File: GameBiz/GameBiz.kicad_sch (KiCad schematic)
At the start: 33 parts

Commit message: initial schematic is finished
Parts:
- removed C? (x2): 10uF, symbol Device:C
- removed L?: 2.2 uH, symbol Device:L
- removed R?: 162K, symbol Device:R
- removed R?: 100K, symbol Device:R
- removed R?: 5.1K, symbol Device:R
- removed S?: RUN, symbol Eclectronics:SW
- removed U?: ADP1607ACPZN001-R7, CP_6_3_ADI, symbol ADP1607ACPZN001:ADP1607ACPZN001-R7
- removed U?: RP2040, Package_DFN_QFN:QFN-56-1EP_7x7mm_P0.4mm_EP3.2x3.2mm, symbol MCU_RaspberryPi:RP2040
- added AE1: Antenna_Loop, Footprints:2_4GHZANTENNA, symbol Device:Antenna_Loop
- added C1, C10, C11, C2, C3, C4, C5, C6, C7, C8, C9: 0.1uF, Capacitor_SMD:C_0603_1608Metric, symbol Device:C
- added C14: 4.7uF, Capacitor_SMD:C_0603_1608Metric, symbol Device:C
- added C16, C18, C20: 100pF, Capacitor_SMD:C_0603_1608Metric, symbol Device:C
- added C17, C19: 2.2uF, Capacitor_SMD:C_0603_1608Metric, symbol Device:C
- added C21: 33nF, Capacitor_SMD:C_0603_1608Metric, symbol Device:C
- added C22: 22uF, Capacitor_SMD:C_0603_1608Metric, symbol Device:C
- added C23: 10nF, Capacitor_SMD:C_0603_1608Metric, symbol Device:C
- added C24: 1nF, Capacitor_SMD:C_0603_1608Metric, symbol Device:C
- added C25, C26: 1uF, Capacitor_SMD:C_0603_1608Metric, symbol Device:C
- added C27: 2.2nF, Capacitor_SMD:C_0603_1608Metric, symbol Device:C
- added C29: 4.7pF, Capacitor_SMD:C_0603_1608Metric, symbol Device:C
- added C30: 1.5pF, Capacitor_SMD:C_0603_1608Metric, symbol Device:C
- added C31: 1pF, Capacitor_SMD:C_0603_1608Metric, symbol Device:C
- added C32: 10uF, Capacitor_SMD:C_0603_1608Metric, symbol Device:C
- added C33, C34: 22pF, Capacitor_SMD:C_0603_1608Metric, symbol Device:C
- added L1: 2.7nH, Inductor_SMD:L_0603_1608Metric, symbol Device:L
- added L2: 3.9nH, Inductor_SMD:L_0603_1608Metric, symbol Device:L
- added L3: 8.2nH, Inductor_SMD:L_0603_1608Metric, symbol Device:L
- added L4: 3.3uH, Inductor_SMD:L_0603_1608Metric, symbol Device:L
- added Q1: PMCXB900UEZ, Footprints:PMCXB900UEZ, symbol PMCXB900UEZ:PMCXB900UEZ
- added R12, R13, R14, R15, R16, R17, R18, R19: 470, Resistor_SMD:R_0603_1608Metric, symbol Device:R
- added R2, R3: 5.1K, Resistor_SMD:R_0603_1608Metric, symbol Device:R
- added R20: 1M, Resistor_SMD:R_0603_1608Metric, symbol Device:R
- added R8: 22K, Resistor_SMD:R_0603_1608Metric, symbol Device:R
- added S1: RST, Footprints:KXT321LHS, symbol Eclectronics:SW
- added S10, S3, S4, S5, S6, S7, S8, S9: SW, Footprints:capacitivetouch, symbol Eclectronics:SW
- added S2: BOOT, Footprints:KXT321LHS, symbol Eclectronics:SW
- added U1: W25Q128JV, Footprints:W25Q128JVPIQ TR, symbol Eclectronics:W25Q128JV
- added U2: RP2040, Footprints:RP2040, symbol Eclectronics:RP2040
- added U6: NRF24L01, Package_DFN_QFN:QFN-20-1EP_4x4mm_P0.5mm_EP2.5x2.5mm, symbol RF:NRF24L01
- added U7: IQS7222A001QNR, Footprints:QFN40P300X300X60-21N, symbol IQS7222A001QNR:IQS7222A001QNR
- added U8: TPS61291DRVT, Footprints:SON65P200X200X80-7N, symbol TPS61291DRVT:TPS61291DRVT
- added U9: EADOGS104NA, Footprints:EADOGS104NA, symbol EADOGS104NA:EADOGS104NA
- added Y1: 12MHz, Footprints:OSC_CSTNE12M0G55A000R0, symbol Eclectronics:Crystal
- added Y2: ECS-160-18-30B-JEM-TR, Footprints:XTAL_ECS-160-18-30B-JEM-TR, symbol ECS-160-18-30B-JEM-TR:ECS-160-18-30B-JEM-TR
- BT1, BT2: renamed from BT?; footprint (none) -> Footprints:24_5mmCoinCell
- C12, C13, C15, C28: renamed from C?; footprint (none) -> Capacitor_SMD:C_0603_1608Metric
- D1, D2: renamed from D?; footprint (none) -> Diode_SMD:D_0603_1608Metric
- D3: renamed from D?; footprint (none) -> LED_SMD:LED_0603_1608Metric
- J1: renamed from J?; footprint GCT_USB4155-03-C_REVA -> Footprints:GCT_USB4155-03-C_REVA
- M1: renamed from M?; footprint XDCR_C0720B001F -> Footprints:XDCR_C0720B001F
- R1, R10, R11, R4, R5, R6, R7, R9: renamed from R?; footprint (none) -> Resistor_SMD:R_0603_1608Metric
- SW1: renamed from SW?; footprint CUS-12TB_NDC -> Footprints:CUS-12TB
- TH1: renamed from TH?; footprint (none) -> Resistor_SMD:R_0603_1608Metric
- U3: renamed from U?; footprint SON65P200X200X80-7N -> Footprints:SON65P200X200X80-7N
- U4: renamed from U?; footprint WSON8_DSG008A_BQ_TEX -> Footprints:BQ25172DSGR
- U5: renamed from U?; footprint PSON50P140X100X40-6N -> Footprints:74LVC1G3157FZ4
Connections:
- net +3.3V: now also M1.1 (V+), C1.1, C14.1, C16.1, C2.2, C23.1, C24.1, C25.1, C3.2, C4.2, C5.2, C6.2, C7.2, C8.2, Q1.4, R2.2, R3.2, U1.8 (VDD), U2.1 (IOVDD), U2.10 (IOVDD), U2.22 (IOVDD), U2.33 (IOVDD), U2.42 (IOVDD), U2.43 (ADC_AVDD), U2.44 (VREG_VIN), U2.48 (USB_VDD), U2.49 (IOVDD), U6.15 (VDD), U6.18 (VDD), U6.7 (VDD), U7.1 (VDD), U9.13 (VDD)
- net GND: now also AE1.1, C1.2, C10.2, C11.1, C14.2, C16.2, C17.2, C18.2, C19.2, C2.1, C20.2, C21.1, C22.1, C23.2, C24.2, C25.2, C26.1, C27.1, C29.1, C3.1, C31.1, C32.2, C33.2, C34.2, C4.1, C5.1, C6.1, C7.1, C8.1, C9.1, Q1.1, R8.1, S1.1, S2.1, U1.4 (GND), U1.9 (EP), U2.19 (TESTEN), U2.57 (GND), U6.14 (VSS), U6.17 (VSS), U6.20 (VSS), U6.8 (VSS), U7.15 (GPIO3), U7.16 (GPIO4), U7.21 (FLOAT), U7.3 (VSSD/VSSA), U8.5 (VSEL), U8.6 (GND), U8.7 (EXP), U9.12 (IM1), U9.14 (VSS), U9.18 (CS), U9.19 (SA0), Y1.2, Y2.2 (GND), Y2.4 (GND)
- net at D2.2 (A), U5.3: now also C22.2, U8.2 (VOUT), U8.4 (EN/BYP)
- net at BT1.1 (+), C28.2, U4.8 (OUT): now also C32.1, L4.2, U8.3 (VIN)
- net at R6.1: now also U2.47 (USB_D+)
- net at R5.2: now also U2.46 (USB_D-)
- net at M1.2 (V-): now also Q1.7, Q1.8
- new net: C33.1, R20.1, U6.10 (XC1), Y2.1 (IN/OUT)
- new net: L4.1, U8.1 (SW)
- new net: R17.1, U7.10 (CRX5)
- new net: R18.1, U7.11 (CRX6)
- new net: R19.1, U7.12 (CRX7)
- new net: S10.1, S3.1, S4.1, S5.1, S6.1, S7.1, S8.1, S9.1, U7.13 (CTX8)
- new net: U2.35 (GPIO23), U7.17 (GPIO5)
- new net: U2.32 (GPIO21), U7.18 (GPIO2), U9.17 (SCLK)
- new net: U2.31 (GPIO20), U7.19 (GPIO1), U9.15 (SOD), U9.16 (SID)
- new net: C17.1, C18.1, U7.2 (VREGD)
- new net: U2.36 (GPIO24), U7.20 (GPIO6)
- new net: C19.1, C20.1, U7.4 (VREGA)
- new net: R12.1, U7.5 (CRX0)
- new net: R13.1, U7.6 (CRX1)
- new net: R14.1, U7.7 (CRX2)
- new net: R15.1, U7.8 (CRX3)
- new net: R16.1, U7.9 (CRX4)
- new net: R17.2, S5.2
- new net: C21.2, U6.19 (DVDD)
- new net: C34.1, R20.2, U6.9 (XC2), Y2.3 (OUT/IN)
- new net: R15.2, S7.2
- new net: R13.2, S9.2
- new net: L2.1, U6.13 (ANT2)
- new net: C30.1, L2.2, L3.1
- new net: R19.2, S3.2
- new net: C10.1, C11.2, C9.2, U2.23 (DVDD), U2.45 (VREG_VOUT), U2.50 (DVDD)
- new net: AE1.2, C30.2, C31.2
- new net: R3.1, S2.2, U1.1 (~{CS}), U2.56 (~{QSPI_CS})
- new net: U1.2 (DO/IO1), U2.55 (QSPI_SD1)
- new net: U1.3 (~{WP}/IO2), U2.54 (QSPI_SD2)
- new net: U1.5 (DI/IO0), U2.53 (QSPI_SD0)
- new net: U1.6 (SCK), U2.52 (QSPI_SCLK)
- new net: U1.7 (~{HOLD}/IO3), U2.51 (QSPI_SD3)
- new net: R18.2, S4.2
- new net: R16.2, S6.2
- new net: R14.2, S8.2
- new net: C26.2, U9.11 (VOUT)
- new net: R12.2, S10.2
- new net: U2.20 (XIN), Y1.1
- new net: U2.21 (XOUT), Y1.3
- new net: R2.1, S1.2, U2.26 (RUN)
- new net: U2.27 (GPIO16), U6.4 (MOSI)
- new net: U2.28 (GPIO17), U6.2 (CSN)
- new net: U2.29 (GPIO18), U6.3 (SCK)
- new net: U2.30 (GPIO19), U6.5 (MISO)
- new net: U2.34 (GPIO22), U6.1 (CE)
- new net: Q1.2, Q1.5, U2.37 (GPIO25)
- new net: C27.2, C29.2, L1.2, L3.2, U6.11 (VDD_PA)
- new net: L1.1, U6.12 (ANT1)
- new net: R8.2, U6.16 (IREF)
- no-connect marks 10 -> 13
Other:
- moved on the sheet: M1, R5, R6

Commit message: layout almost finished
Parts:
- removed TH1: Thermistor, Resistor_SMD:R_0603_1608Metric, symbol Device:Thermistor
- added R12: 10K, Resistor_SMD:R_0603_1608Metric, symbol Device:R
- renumbered R12 to R13, R13 to R14, R14 to R15, R15 to R16, R16 to R17, R17 to R18, R18 to R19, R19 to R20, R20 to R21
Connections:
- net GND: now also R12.1
- net at D1.1 (K), U5.5 (VCC): now also D2.1 (K)
- net at U4.3 (TS): now also R12.2
- no-connect marks 13 -> 15
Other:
- moved on the sheet: D1, D2

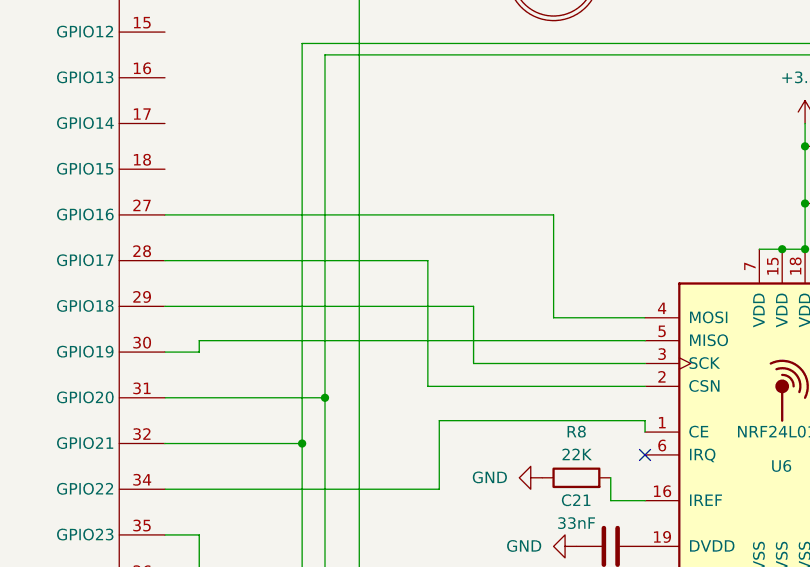
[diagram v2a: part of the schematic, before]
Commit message: capacitive buttons need to be finished
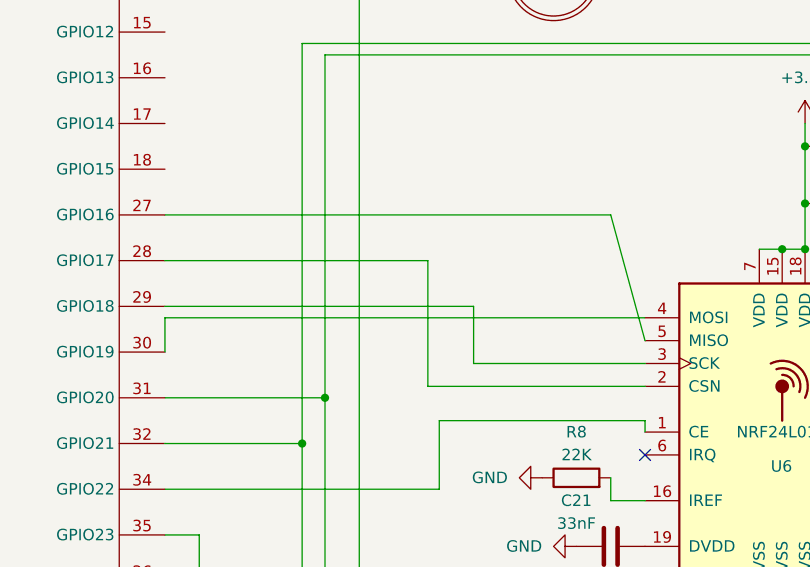
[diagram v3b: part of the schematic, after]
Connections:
- net at U2.27 (GPIO16): now also U6.5 (MISO); no longer U6.4 (MOSI)
- net at U2.30 (GPIO19): now also U6.4 (MOSI); no longer U6.5 (MISO)
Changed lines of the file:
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@@
+    (stroke (width 0) (type default) (color 0 0 0 0))
+  )
+  (wire (pts (xy 199.39 163.83) (xy 203.2 177.8))
     (stroke (width 0) (type default) (color 0 0 0 0))
   )
@@
     (stroke (width 0) (type default) (color 0 0 0 0))
   )
-  (wire (pts (xy 153.67 179.07) (xy 149.86 179.07))
-    (stroke (width 0) (type default) (color 0 0 0 0))
-  )
   (wire (pts (xy 224.79 109.22) (xy 228.6 109.22))
     (stroke (width 0) (type default) (color 0 0 0 0))
@@
     (stroke (width 0) (type default) (color 0 0 0 0))
   )
-  (wire (pts (xy 203.2 175.26) (xy 193.04 175.26))
+  (wire (pts (xy 149.86 175.26) (xy 203.2 175.26))
     (stroke (width 0) (type default) (color 0 0 0 0))
   )
@@
     (stroke (width 0) (type default) (color 0 0 0 0))
   )
-  (wire (pts (xy 203.2 177.8) (xy 153.67 177.8))
+  (wire (pts (xy 199.39 163.83) (xy 149.86 163.83))
     (stroke (width 0) (type default) (color 0 0 0 0))
   )
@@
     (stroke (width 0) (type default) (color 0 0 0 0))
   )
-  (wire (pts (xy 193.04 175.26) (xy 193.04 163.83))
-    (stroke (width 0) (type default) (color 0 0 0 0))
-  )
   (wire (pts (xy 67.31 138.43) (xy 88.9 138.43))
     (stroke (width 0) (type default) (color 0 0 0 0))
@@
     (stroke (width 0) (type default) (color 0 0 0 0))
   )
+  (wire (pts (xy 149.86 175.26) (xy 149.86 179.07))
+    (stroke (width 0) (type default) (color 0 0 0 0))
+  )
   (wire (pts (xy 241.3 163.83) (xy 246.38 163.83))
     (stroke (width 0) (type default) (color 0 0 0 0))
@@
     (stroke (width 0) (type default) (color 0 0 0 0))
   )
-  (wire (pts (xy 153.67 177.8) (xy 153.67 179.07))
-    (stroke (width 0) (type default) (color 0 0 0 0))
-  )
   (wire (pts (xy 153.67 53.34) (xy 196.85 53.34))
     (stroke (width 0) (type default) (color 0 0 0 0))
@@
     (stroke (width 0) (type default) (color 0 0 0 0))
   )
-  (wire (pts (xy 193.04 163.83) (xy 149.86 163.83))
-    (stroke (width 0) (type default) (color 0 0 0 0))
-  )

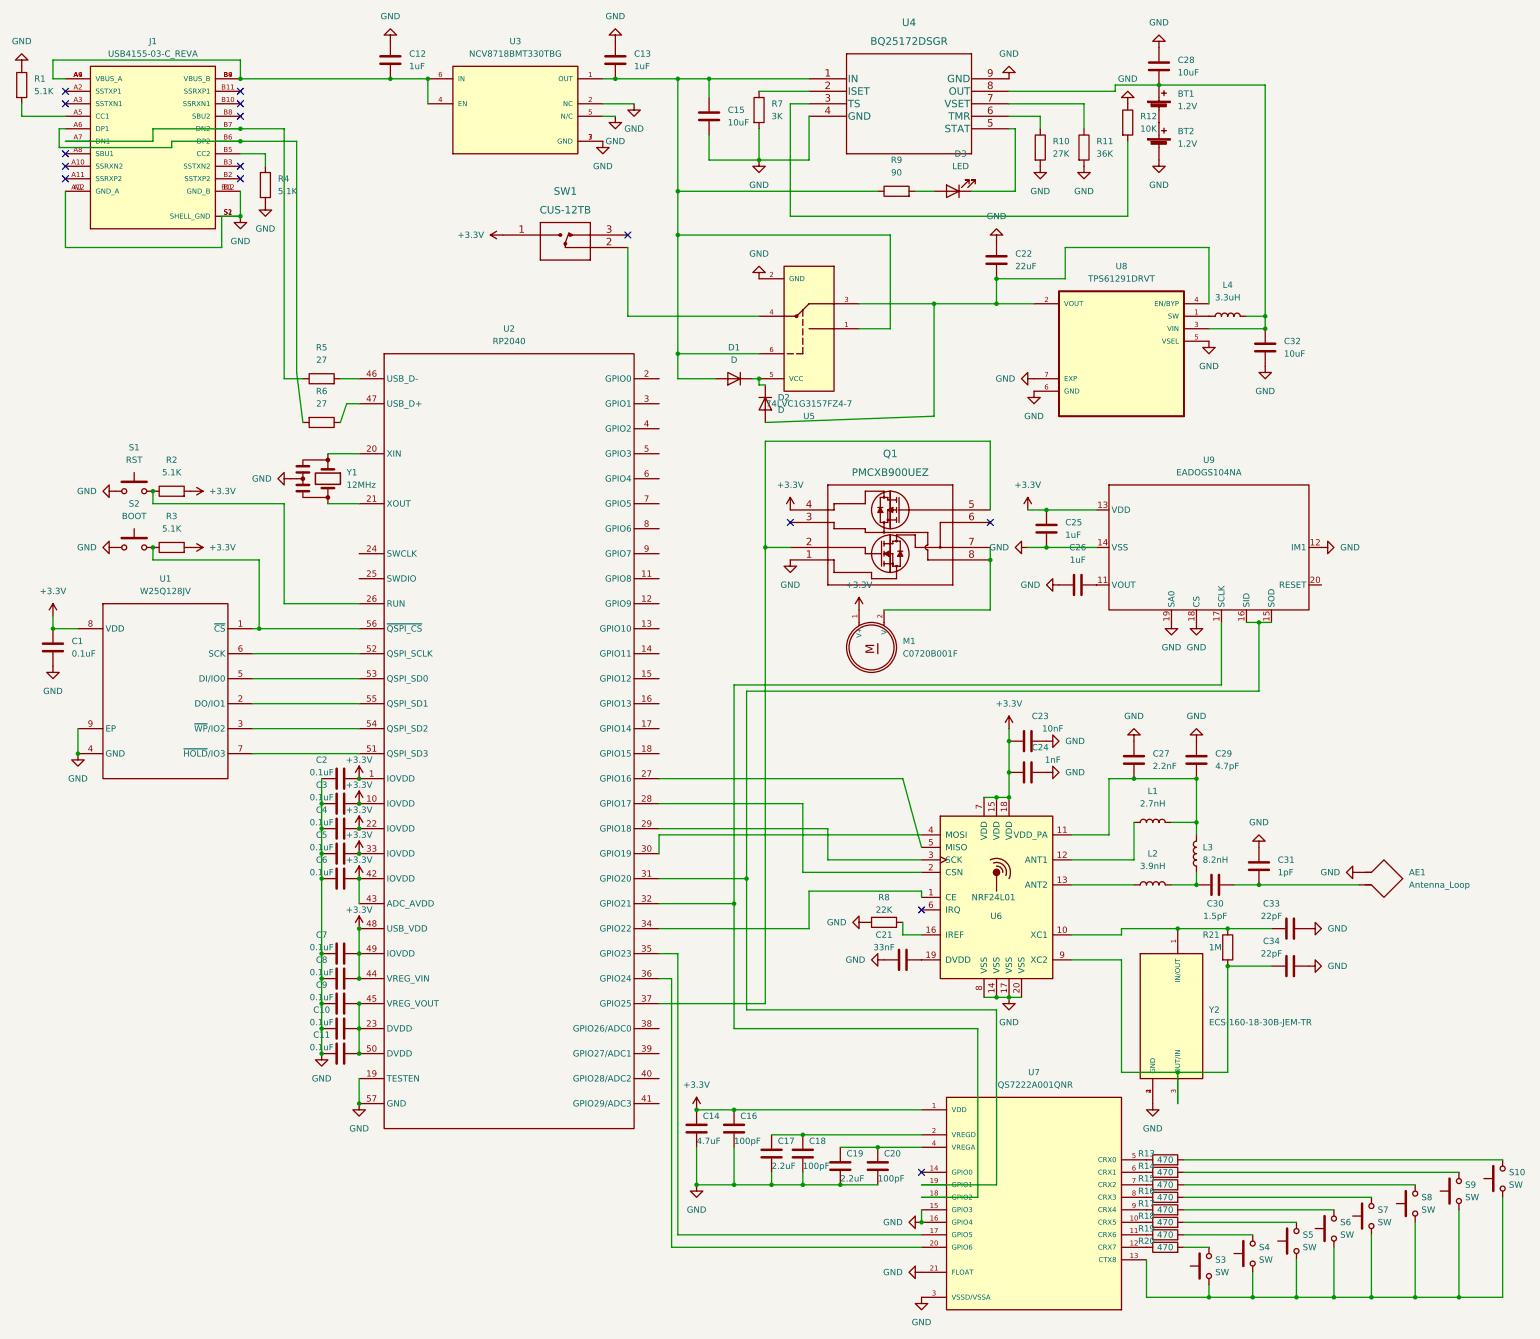
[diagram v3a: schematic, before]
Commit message: finished initial layout, still some errors
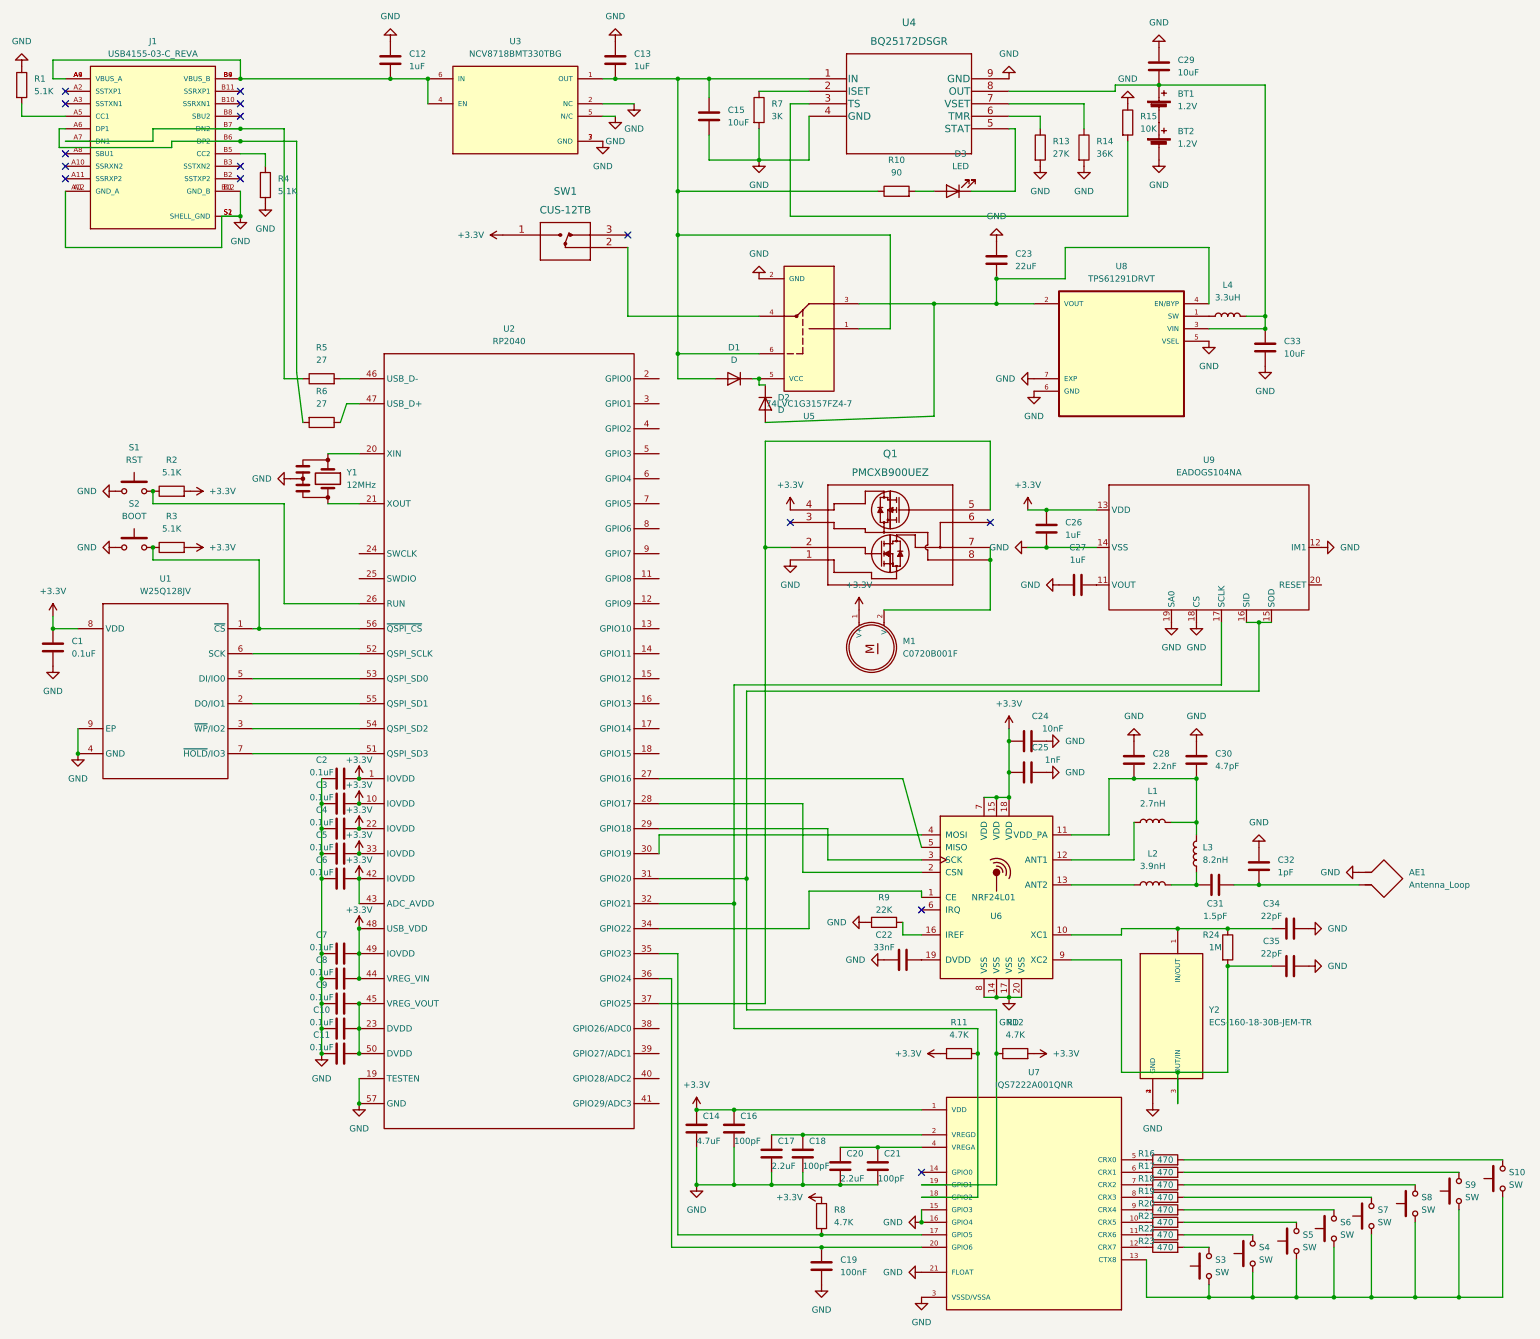
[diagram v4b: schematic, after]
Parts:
- added C19: 100nF, Capacitor_SMD:C_0603_1608Metric, symbol Device:C
- added R11, R12, R8: 4.7K, Resistor_SMD:R_0603_1608Metric, symbol Device:R
- renumbered C19 to C20, C20 to C21, C21 to C22, C22 to C23, C23 to C24, C24 to C25, C25 to C26, C26 to C27, C27 to C28, C28 to C29, C29 to C30, C30 to C31, C31 to C32, C32 to C33, C33 to C34, C34 to C35, R9 to R10, R10 to R13, R11 to R14, R12 to R15, R13 to R16, R14 to R17, R15 to R18, R16 to R19, R17 to R20, R18 to R21, R19 to R22, R20 to R23, R21 to R24, R8 to R9
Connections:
- net +3.3V: now also R11.1, R12.2, R8.1
- net GND: now also C19.2
- net at U2.35 (GPIO23), U7.17 (GPIO5): now also R8.2
- net at U2.32 (GPIO21), U7.18 (GPIO2), U9.17 (SCLK): now also R11.2
- net at U2.31 (GPIO20), U7.19 (GPIO1), U9.15 (SOD)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: now also R12.1
- net at U2.36 (GPIO24), U7.20 (GPIO6): now also C19.1
